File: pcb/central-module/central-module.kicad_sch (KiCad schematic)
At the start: 28 parts, among them J1 Conn_01x10_Pin, J2 Screw_Terminal_01x04, J3 Conn_01x04_Pin, J4 Screw_Terminal_01x03, J5 Screw_Terminal_01x04, Q1 IRF3205, U1 ESP32_DEVCITV1, U2 74HC245

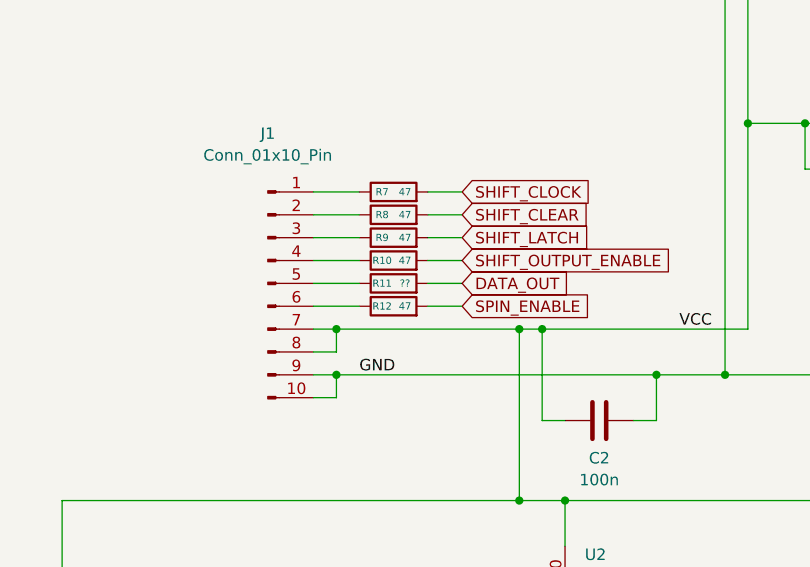
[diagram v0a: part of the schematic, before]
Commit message: central-module.kicad_sch -> kicad 9
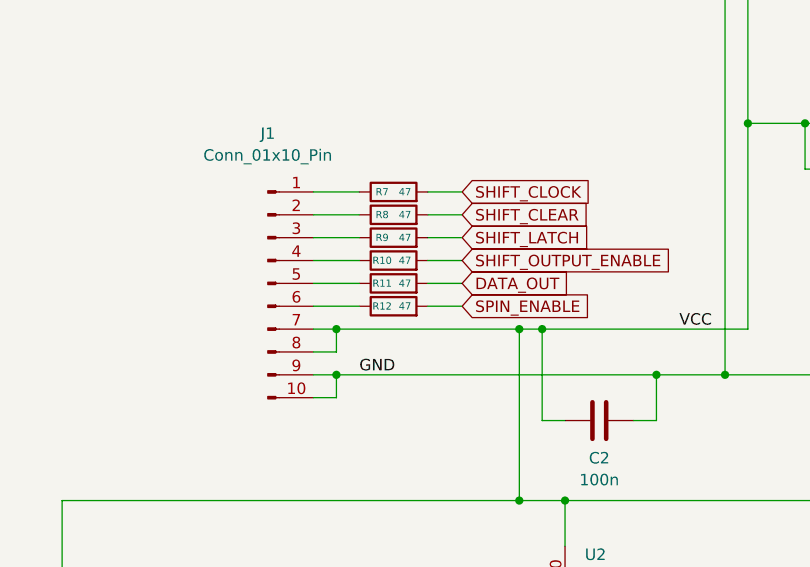
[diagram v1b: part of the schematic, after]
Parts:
- R11: value ?? -> 47
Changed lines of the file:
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@@
 (kicad_sch
-	(version 20231120)
+	(version 20250114)
 	(generator "eeschema")
-	(generator_version "8.0")
+	(generator_version "9.0")
 	(paper "A4")
+	(text "~"
+		(exclude_from_sim no)
+		(at 38.1 83.82 0)
+		(effects
+			(font
+				(size 2.54 2.54)
+				(thickness 0.508)
+				(bold yes)
+			)
+		)
+	)
+	(text "+24V DC"
+		(exclude_from_sim no)
+		(at 52.07 47.498 0)
+		(effects
+			(font
+				(size 1.27 1.27)
+				(thickness 0.254)
+				(bold yes)
+			)
+		)
+	)
+	(text "Pulldown SPIN_ENABLE"
+		(exclude_from_sim no)
+		(at 198.374 125.984 0)
+		(effects
+			(font
+				(size 1.27 1.27)
+			)
+		)
+	)
+	(text "~"
+		(exclude_from_sim no)
+		(at 39.878 83.82 0)
+		(effects
+			(font
+				(size 1.27 1.27)
+			)
+		)
+	)
+	(text "24 V AC"
+		(exclude_from_sim no)
+		(at 259.08 35.814 0)
+		(effects
+			(font
+				(size 1.27 1.27)
+				(bold yes)
+			)
+		)
+	)
+	(text " ~ "
+		(exclude_from_sim no)
+		(at 39.116 83.82 0)
+		(effects
+			(font
+				(size 2.54 2.54)
+				(bold yes)
+			)
+		)
+	)
+	(text "24 V DC"
+		(exclude_from_sim no)
+		(at 259.08 40.894 0)
+		(effects
+			(font
+				(size 1.27 1.27)
+				(bold yes)
+			)
+		)
+	)
+	(text "75HCT245"
+		(exclude_from_sim no)
+		(at 103.124 152.146 0)
+		(effects
+			(font
+				(size 1.27 1.27)
+			)
+		)
+	)
+	(text "230 V AC Netz"
+		(exclude_from_sim no)
+		(at 27.94 83.82 0)
+		(effects
+			(font
+				(size 1.5 1.5)
+				(bold yes)
+			)
+		)
+	)
+	(text "+5V DC"
+		(exclude_from_sim no)
+		(at 51.562 49.784 0)
+		(effects
+			(font
+				(size 1.27 1.27)
+				(thickness 0.254)
+				(bold yes)
+			)
+		)
+	)
+	(text "Trafo Primär"
+		(exclude_from_sim no)
+		(at 26.67 79.248 0)
+		(effects
+			(font
+				(size 1.5 1.5)
+				(bold yes)
+			)
+		)
+	)
+	(text " ~ "
+		(exclude_from_sim no)
+		(at 39.116 79.248 0)
+		(effects
+			(font
+				(size 2.54 2.54)
+				(bold yes)
+			)
+		)
+	)
+	(text "Pullup SHIFT_OUTPUT_ENABLE"
+		(exclude_from_sim no)
+		(at 196.088 106.68 0)
+		(effects
+			(font
+				(size 1.27 1.27)
+			)
+		)
+	)
+	(text "GND"
+		(exclude_from_sim no)
+		(at 52.07 52.324 0)
+		(effects
+			(font
+				(size 1.27 1.27)
+				(thickness 0.254)
+				(bold yes)
+			)
+			(href "#1")
+		)
+	)
+	(text "Trafo Sekundär"
+		(exclude_from_sim no)
+		(at 41.656 33.528 0)
+		(effects
+			(font
+				(size 2.54 2.54)
+				(bold yes)
+			)
+		)
+	)
 	(junction
 		(at 106.68 101.6)
@@
 		)
 	)
-	(text "~"
-		(exclude_from_sim no)
-		(at 38.1 83.82 0)
-		(effects
-			(font
-				(size 2.54 2.54)
-				(thickness 0.508)
-				(bold yes)
-			)
-		)
-	)
-	(text "+24V DC"
-		(exclude_from_sim no)
-		(at 52.07 47.498 0)
-		(effects
-			(font
-				(size 1.27 1.27)
-				(thickness 0.254)
-				(bold yes)
-			)
-		)
-	)
-	(text "Pulldown SPIN_ENABLE"
-		(exclude_from_sim no)
-		(at 198.374 125.984 0)
-		(effects
-			(font
-				(size 1.27 1.27)
-			)
-		)
-	)
-	(text "~"
-		(exclude_from_sim no)
-		(at 39.878 83.82 0)
-		(effects
-			(font
-				(size 1.27 1.27)
-			)
-		)
-	)
-	(text "24 V AC"
-		(exclude_from_sim no)
-		(at 259.08 35.814 0)
-		(effects
-			(font
-				(size 1.27 1.27)
-				(bold yes)
-			)
-		)
-	)
-	(text " ~ "
-		(exclude_from_sim no)
-		(at 39.116 83.82 0)
-		(effects
-			(font
-				(size 2.54 2.54)
-				(bold yes)
-			)
-		)
-	)
-	(text "24 V DC"
-		(exclude_from_sim no)
-		(at 259.08 40.894 0)
-		(effects
-			(font
-				(size 1.27 1.27)
-				(bold yes)
-			)
-		)
-	)
-	(text "75HCT245"
-		(exclude_from_sim no)
-		(at 103.124 152.146 0)
-		(effects
-			(font
-				(size 1.27 1.27)
-			)
-		)
-	)
-	(text "230 V AC Netz"
-		(exclude_from_sim no)
-		(at 27.94 83.82 0)
-		(effects
-			(font
-				(size 1.5 1.5)
-				(bold yes)
-			)
-		)
-	)
-	(text "+5V DC"
-		(exclude_from_sim no)
-		(at 51.562 49.784 0)
-		(effects
-			(font
-				(size 1.27 1.27)
-				(thickness 0.254)
-				(bold yes)
-			)
-		)
-	)
-	(text "Trafo Primär"
-		(exclude_from_sim no)
-		(at 26.67 79.248 0)
-		(effects
-			(font
-				(size 1.5 1.5)
-				(bold yes)
-			)
-		)
-	)
-	(text " ~ "
-		(exclude_from_sim no)
-		(at 39.116 79.248 0)
-		(effects
-			(font
-				(size 2.54 2.54)
-				(bold yes)
-			)
-		)
-	)
-	(text "Pullup SHIFT_OUTPUT_ENABLE"
-		(exclude_from_sim no)
-		(at 196.088 106.68 0)
-		(effects
-			(font
-				(size 1.27 1.27)
-			)
-		)
-	)
-	(text "GND"
-		(exclude_from_sim no)
-		(at 52.07 52.324 0)
-		(effects
-			(font
-				(size 1.27 1.27)
-				(thickness 0.254)
-				(bold yes)
-			)
-			(href "#1")
-		)
-	)
-	(text "Trafo Sekundär"
-		(exclude_from_sim no)
-		(at 41.656 33.528 0)
-		(effects
-			(font
-				(size 2.54 2.54)
-				(bold yes)
-			)
-		)
-	)
 	(label "N"
 		(at 49.53 82.55 0)
-		(fields_autoplaced yes)
 		(effects
 			(font
@@
 	(label "24VAC_N"
 		(at 240.03 36.83 0)
-		(fields_autoplaced yes)
 		(effects
 			(font
@@
 	(label "P"
 		(at 49.53 85.09 0)
-		(fields_autoplaced yes)
 		(effects
 			(font
@@
 	(label "GND"
 		(at 63.5 129.54 0)
-		(fields_autoplaced yes)
 		(effects
 			(font
@@
 	(label "24VAC_P"
 		(at 240.03 34.29 0)
-		(fields_autoplaced yes)
 		(effects
 			(font
@@
 	(label "VCC"
 		(at 99.06 124.46 0)
-		(fields_autoplaced yes)
 		(effects
 			(font
@@
 	(label "24VAC_P_UF"
 		(at 73.66 29.21 0)
-		(fields_autoplaced yes)
 		(effects
 			(font
@@
 	(label "T_BRIDGE"
 		(at 71.12 31.75 0)
-		(fields_autoplaced yes)
 		(effects
 			(font
@@
 	(label "P_FUSED"
 		(at 62.23 69.85 0)
-		(fields_autoplaced yes)
 		(effects
 			(font
@@
 	(label "+24V_UF"
 		(at 71.12 46.99 0)
-		(fields_autoplaced yes)
 		(effects
 			(font
@@
 			)
 		)
-		(property "Value" "??"
+		(property "Value" "47"
 			(at 68.58 119.38 90)
 			(effects
@@
 		)
 	)
+	(embedded_fonts no)
 )

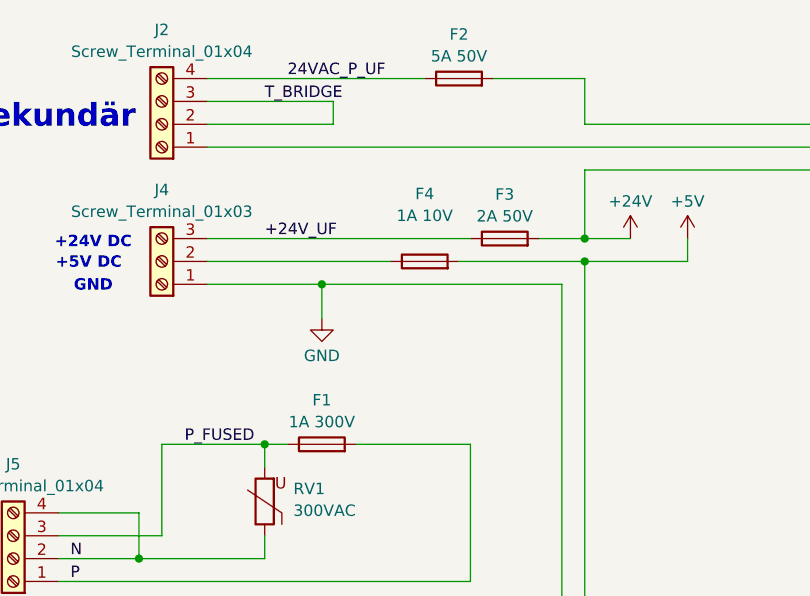
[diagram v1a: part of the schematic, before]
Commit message: full 20 module current measurement and fuses
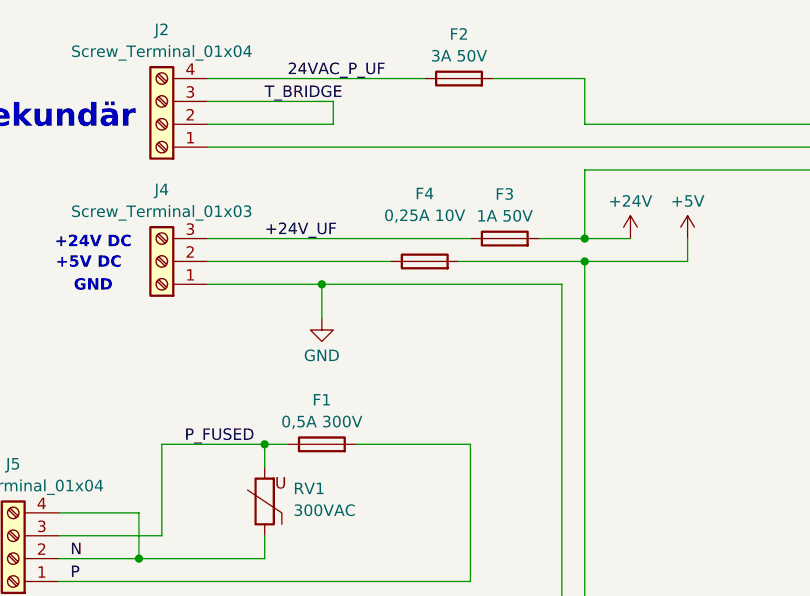
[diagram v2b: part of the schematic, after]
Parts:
- F1: value 1A 300V -> 0,5A 300V
- F2: value 5A 50V -> 3A 50V
- F3: value 2A 50V -> 1A 50V
- F4: value 1A 10V -> 0,25A 10V
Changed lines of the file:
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@@
 			)
 		)
-		(property "Value" "5A 50V"
+		(property "Value" "3A 50V"
 			(at 92.71 26.7278 90)
 			(effects
@@
 			)
 		)
-		(property "Value" "2A 50V"
+		(property "Value" "1A 50V"
 			(at 97.79 44.5078 90)
 			(effects
@@
 			)
 		)
-		(property "Value" "1A 10V"
+		(property "Value" "0,25A 10V"
 			(at 88.9 44.45 90)
 			(effects
@@
 			)
 		)
-		(property "Value" "1A 300V"
+		(property "Value" "0,5A 300V"
 			(at 77.47 67.3678 90)
 			(effects

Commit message: new terminal blocks 7.5 and schurter fuseholders
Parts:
- F1, F2, F3, F4: footprint Fuse:Fuseholder_Littelfuse_445_030_series_5x20mm -> JS_Local:Fuseholder_Schurter_OGN_22.5
- J2, J5: footprint TerminalBlock_MetzConnect:TerminalBlock_MetzConnect_Type011_RT05504HBWC_1x04_P5.00mm_Horizontal -> TerminalBlock_MetzConnect:TerminalBlock_MetzConnect_Type175_RT02704HBLC_1x04_P7.50mm_Horizontal
- J4: footprint TerminalBlock_MetzConnect:TerminalBlock_MetzConnect_Type011_RT05503HBWC_1x03_P5.00mm_Horizontal -> TerminalBlock_MetzConnect:TerminalBlock_MetzConnect_Type011_RT05503HBLC_1x03_P5.00mm_Horizontal
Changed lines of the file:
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@@
 			)
 		)
-		(property "Footprint" "Fuse:Fuseholder_Littelfuse_445_030_series_5x20mm"
+		(property "Footprint" "JS_Local:Fuseholder_Schurter_OGN_22.5"
 			(at 92.71 30.988 90)
 			(effects
@@
 			)
 		)
-		(property "Footprint" "Fuse:Fuseholder_Littelfuse_445_030_series_5x20mm"
+		(property "Footprint" "JS_Local:Fuseholder_Schurter_OGN_22.5"
 			(at 97.79 48.768 90)
 			(effects
@@
 			)
 		)
-		(property "Footprint" "TerminalBlock_MetzConnect:TerminalBlock_MetzConnect_Type011_RT05504HBWC_1x04_P5.00mm_Horizontal"
+		(property "Footprint" "TerminalBlock_MetzConnect:TerminalBlock_MetzConnect_Type175_RT02704HBLC_1x04_P7.50mm_Horizontal"
 			(at 59.69 34.29 0)
 			(effects
@@
 			)
 		)
-		(property "Footprint" "TerminalBlock_MetzConnect:TerminalBlock_MetzConnect_Type011_RT05504HBWC_1x04_P5.00mm_Horizontal"
+		(property "Footprint" "TerminalBlock_MetzConnect:TerminalBlock_MetzConnect_Type175_RT02704HBLC_1x04_P7.50mm_Horizontal"
 			(at 43.18 82.55 0)
 			(effects
@@
 			)
 		)
-		(property "Footprint" "TerminalBlock_MetzConnect:TerminalBlock_MetzConnect_Type011_RT05503HBWC_1x03_P5.00mm_Horizontal"
+		(property "Footprint" "TerminalBlock_MetzConnect:TerminalBlock_MetzConnect_Type011_RT05503HBLC_1x03_P5.00mm_Horizontal"
 			(at 59.69 49.53 0)
 			(effects
@@
 			)
 		)
-		(property "Footprint" "Fuse:Fuseholder_Littelfuse_445_030_series_5x20mm"
+		(property "Footprint" "JS_Local:Fuseholder_Schurter_OGN_22.5"
 			(at 88.9 51.308 90)
 			(effects
@@
 			)
 		)
-		(property "Footprint" "Fuse:Fuseholder_Littelfuse_445_030_series_5x20mm"
+		(property "Footprint" "JS_Local:Fuseholder_Schurter_OGN_22.5"
 			(at 77.47 71.628 90)
 			(effects
